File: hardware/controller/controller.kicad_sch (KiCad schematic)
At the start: 142 parts

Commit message: Update controller designs to KiCAD v7
Change-Id: I1269c7bbf32ea052580bc09d77739b31cda08142
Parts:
- C1, C10, C15, C2, C21, C22, C23, C24, C25, C3, C4, C5, C6, C7, C8: value (none) -> 0.1uF; footprint (none) -> Capacitor_SMD:C_0402_1005Metric_Pad0.74x0.62mm_HandSolder
- C11, C12, C13, C14, C16, C17, C18, C20, C9: value (none) -> 4.7uF; footprint (none) -> Capacitor_SMD:C_0603_1608Metric
- C19: value (none) -> 1pF; footprint (none) -> Capacitor_SMD:C_0402_1005Metric_Pad0.74x0.62mm_HandSolder
- D1, D2, D26, D3, D30, D31, D4, D46, D50, D51: value (none) -> D_TVS; footprint (none) -> Diode_SMD:D_SOD-323
- D10, D11, D12, D13, D14, D15, D16, D17, D18, D19, D20, D21, D22, D23, D24, D25, D27, D28, D29, D32, D33, D34, D36, D37, D38, D40, D41, D42, D43, D44, D45, D47, D48, D49, D5, D6, D7, D8, D9: value (none) -> WS2812B; footprint (none) -> LED_SMD:LED_WS2812B_PLCC4_5.0x5.0mm_P3.2mm
- D35: value (none) -> GREEN; footprint (none) -> LED_SMD:LED_0603_1608Metric
- D39: value (none) -> RED; footprint (none) -> LED_SMD:LED_0603_1608Metric
- H1, H2, H3, H4: value (none) -> MountingHole; footprint (none) -> MountingHole:MountingHole_3.2mm_M3
- J1: value (none) -> Conn_01x05; footprint (none) -> Connector_PinHeader_2.54mm:PinHeader_1x05_P2.54mm_Vertical
- J2, J5: value (none) -> Conn_01x03; footprint (none) -> Connector_PinHeader_2.54mm:PinHeader_1x03_P2.54mm_Horizontal
- J3: value (none) -> Conn_01x04; footprint (none) -> Connector_PinHeader_2.54mm:PinHeader_1x04_P2.54mm_Vertical
- J4: value (none) -> USB_B_Micro; footprint (none) -> homebrew:FRAMATOME_10118194-0001LF_fixed_bridges
- JP1, JP2: value (none) -> SolderJumper_2_Open; footprint (none) -> Jumper:SolderJumper-2_P1.3mm_Open_RoundedPad1.0x1.5mm
- L1: value (none) -> 10nH; footprint (none) -> Inductor_SMD:L_0402_1005Metric
- R1, R11, R25, R35, R7: value (none) -> 33R; footprint (none) -> Resistor_SMD:R_0603_1608Metric
- R10, R13, R6: value (none) -> 100R; footprint (none) -> Resistor_SMD:R_0603_1608Metric
- R12, R14, R15, R16, R17, R18, R22, R23, R24: value (none) -> 0R; footprint (none) -> Resistor_SMD:R_0603_1608Metric
- R19, R26, R3: value (none) -> 47k; footprint (none) -> Resistor_SMD:R_0603_1608Metric
- R2: value (none) -> 470k; footprint (none) -> Resistor_SMD:R_0603_1608Metric
- R20, R27, R34, R4: value (none) -> 24k; footprint (none) -> Resistor_SMD:R_0603_1608Metric
- R21, R28, R5: value (none) -> 68k; footprint (none) -> Resistor_SMD:R_0603_1608Metric
- R29: value (none) -> 62k; footprint (none) -> Resistor_SMD:R_0603_1608Metric
- R30: value (none) -> 180k; footprint (none) -> Resistor_SMD:R_0603_1608Metric
- R31, R32: value (none) -> 1k; footprint (none) -> Resistor_SMD:R_0603_1608Metric
- R33: value (none) -> 3k3; footprint (none) -> Resistor_SMD:R_0603_1608Metric
- R8: value (none) -> 240k; footprint (none) -> Resistor_SMD:R_0603_1608Metric
- R9: value (none) -> 680k; footprint (none) -> Resistor_SMD:R_0603_1608Metric
- S1: value (none) -> OS103011MS8QP1; footprint (none) -> snapeda:OS102011MS8QP1
- SW1, SW2, SW3, SW4, SW5, SW6, SW7, SW8, SW9: value (none) -> ILS_TA180_50; footprint (none) -> homebrew:SW_CK_TA
- SW10: value (none) -> SW_SPDT; footprint (none) -> homebrew:ANR11R11P2HQE
- TH1: value (none) -> Thermistor_PTC; footprint (none) -> Fuse:Fuse_1206_3216Metric_Pad1.42x1.75mm_HandSolder
- U1, U3, U4: value (none) -> WS2811; footprint (none) -> Package_SO:SOP-8_3.9x4.9mm_P1.27mm
- U2: value (none) -> STM32F103C8Tx; footprint (none) -> Package_QFP:LQFP-48_7x7mm_P0.5mm
- U5: value (none) -> HT75xx-1-SOT89; footprint (none) -> Package_TO_SOT_SMD:SOT-89-3
- U6: value (none) -> RFM69CW-915MHZ; footprint (none) -> homebrew:RFM69CW-minimalpads
- U7: value (none) -> TP4056; footprint (none) -> snapeda:SOP127P600X175-9N

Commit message: Schematic update for controller v1.1:
- Switch to WS2812C (low-power)
- Switch to JLC-placed TVS diodes
- Actually connect mode switch to micro
- Switch to STM32G070
- Reduce filter caps on analog buttons
- Add microphone
- Add FRAM
- Fix charge status LEDs
- Change to smaller power switch
- Add reset button
- Remove unneeded resistors on button LEDs
- Switch to smaller CH340X

Change-Id: I1a39cd43177c431c6a7b54ff1605266b9eb21616
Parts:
- removed C21, C22: 0.1uF, Capacitor_SMD:C_0402_1005Metric_Pad0.74x0.62mm_HandSolder, symbol Device:C
- removed D46, D50, D51: D_TVS, Diode_SMD:D_SOD-323, symbol Device:D_TVS
- removed JP1, JP2: SolderJumper_2_Open, Jumper:SolderJumper-2_P1.3mm_Open_RoundedPad1.0x1.5mm, symbol Jumper:SolderJumper_2_Open
- removed R16, R17, R18, R22, R23, R24: 0R, Resistor_SMD:R_0603_1608Metric, symbol Device:R
- removed R34: 24k, Resistor_SMD:R_0603_1608Metric, symbol Device:R
- removed SW10: SW_SPDT, homebrew:ANR11R11P2HQE, symbol Switch:SW_SPDT
- removed U2: STM32F103C8Tx, Package_QFP:LQFP-48_7x7mm_P0.5mm, symbol MCU_ST_STM32F1:STM32F103C8Tx
- added C21, C22, C28: 100uF, Capacitor_SMD:CP_Elec_6.3x5.4, symbol Device:C_Polarized
- added C26, C27, C29, C30, C31, C32, C33, C34, C35, C36, C37, C38, C39, C40, C41, C42, C43, C44, C45, C46, C47, C48, C49, C50, C51, C52, C53, C54, C55, C56, C57, C58, C59, C60, C61, C62, C63, C64, C65, C66, C67: 100nF, Capacitor_SMD:C_0402_1005Metric_Pad0.74x0.62mm_HandSolder, symbol Device:C
- added D46: SRV05-4-P-T7, Package_TO_SOT_SMD:SOT-23-6, symbol Homebrew:SRV05-4-P-T7
- added D52: D, Diode_SMD:D_SMA, symbol Device:D
- added J6: Conn_01x02, Homebrew:JST_Micro_1x02_P1.25mm_Horizontal, symbol Connector_Generic:Conn_01x02
- added MK1: Microphone, Homebrew:MIC_CMA-4544PF-W, symbol Device:Microphone
- added Q1: MMBT2222A 1P, Package_TO_SOT_SMD:SOT-23, symbol Transistor_BJT:MMBT3904
- added Q2: AO3400A, Package_TO_SOT_SMD:SOT-23, symbol Transistor_FET:AO3400A
- added R36: 1k, Resistor_SMD:R_0603_1608Metric, symbol Device:R
- added R38, R39: 220, Resistor_SMD:R_0402_1005Metric, symbol Device:R
- added R40, R41: 3k3, Resistor_SMD:R_0603_1608Metric, symbol Device:R
- added R42, R44: 2k2, Resistor_SMD:R_0603_1608Metric_Pad0.98x0.95mm_HandSolder, symbol Device:R
- added R43: 6k8, Resistor_SMD:R_0603_1608Metric_Pad0.98x0.95mm_HandSolder, symbol Device:R
- added R45: 220, Resistor_SMD:R_0603_1608Metric_Pad0.98x0.95mm_HandSolder, symbol Device:R
- added R46: 1k, Resistor_SMD:R_0603_1608Metric_Pad0.98x0.95mm_HandSolder, symbol Device:R
- added SW10: SW_Push, Homebrew:SW_TACTILE_5.1MM_TS-1187A-C-D-B, symbol Switch:SW_Push
- added SW11: SW_DPDT_x2, Homebrew:SK22D15L5_SP, symbol Switch:SW_DPDT_x2
- added U10: CH340X, Package_SO:MSOP-10_3x3mm_P0.5mm, symbol Interface_USB:CH340E
- added U2: FM24CL16B, Package_SO:SOIC-8_3.9x4.9mm_P1.27mm, symbol Memory_NVRAM:FM24CL16B
- added U8: STM32G070CBTx, Package_QFP:LQFP-48_7x7mm_P0.5mm, symbol MCU_ST_STM32G0:STM32G070CBTx
- C1, C10, C15, C23, C25, C3, C5, C6, C7: value 0.1uF -> 100nF
- C11, C12, C13, C14, C16, C17, C18, C9: value 4.7uF -> 10uF; LCSC C19666 -> C96446
- C2, C4, C8: value 0.1uF -> 22nF; LCSC C307331 -> C1532
- C20: value 4.7uF -> 100nF; footprint Capacitor_SMD:C_0603_1608Metric -> Capacitor_SMD:C_0402_1005Metric_Pad0.74x0.62mm_HandSolder; LCSC C19666 -> C307331
- C24: value 0.1uF -> 10nF; footprint Capacitor_SMD:C_0402_1005Metric_Pad0.74x0.62mm_HandSolder -> Capacitor_SMD:C_0603_1608Metric_Pad1.08x0.95mm_HandSolder; LCSC C307331 -> C85973
- D1, D2, D26, D3, D30, D31, D4: LCSC (none) -> C127522; MPN DESD5V0U1BA-7 -> (none)
- D10, D11, D12, D13, D14, D15, D16, D17, D18, D19, D20, D21, D22, D23, D24, D25, D27, D28, D29, D32, D33, D34, D36, D37, D38, D40, D41, D42, D43, D44, D45, D47, D48, D49, D5, D6, D7, D8, D9: value WS2812B -> WS2812C/W; LCSC C2761795 -> C2761796
- D35: value GREEN -> WHITE; LCSC (none) -> C2290; MPN LTST-C190KGKT -> (none)
- R1, R11, R25, R35, R7: value 33R -> 33
- R10, R13, R6: value 100R -> 100
- R12: value 0R -> 220; footprint Resistor_SMD:R_0603_1608Metric -> Resistor_SMD:R_0402_1005Metric; LCSC C21189 -> C25091
- R14: value 0R -> 10k; footprint Resistor_SMD:R_0603_1608Metric -> Resistor_SMD:R_0402_1005Metric; LCSC C21189 -> C25744
- R15: value 0R -> 4k7; footprint Resistor_SMD:R_0603_1608Metric -> Resistor_SMD:R_0402_1005Metric; LCSC C21189 -> C25900
- S1: footprint snapeda:OS102011MS8QP1 -> OS102011MS8QP1
- TH1: footprint Fuse:Fuse_1206_3216Metric_Pad1.42x1.75mm_HandSolder -> Fuse:Fuse_0805_2012Metric; LCSC (none) -> C269105; MPN PTS12066V100 -> (none)
- U6: footprint homebrew:RFM69CW-minimalpads -> RFM69CW-XXXS2
- U7: footprint snapeda:SOP127P600X175-9N -> SOP127P600X175-9N
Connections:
- net SWCLK is gone; now on net BOOT0: J3.4 (Pin_4)
- net +BATT: now also J5.3 (Pin_3), C29.1, C30.1, C31.1, C32.1, C33.1, C34.1, C35.1, C36.1, C37.1, C38.1, C39.1, C40.1, C41.1, C42.1, C43.1, C44.1, C45.1, C46.1, C47.1, C48.1, C49.1, C50.1, C51.1, C52.1, C53.1, C54.1, C55.1, C56.1, C57.1, C58.1, C59.1, C60.1, C61.1, C62.1, C63.1, C64.1, C65.1, C66.1, C67.1, D52.1 (K), SW11.1 (A), SW11.4 (A); no longer J5.1 (Pin_1)
- net AUX0: now also J1.4 (Pin_4), U8.22 (PB10); no longer J1.2 (Pin_2)
- net AUX1: now also J1.5 (Pin_5), U8.23 (PB11); no longer J1.1 (Pin_1)
- net BATT_DIRECT: now also SW11.2 (B), SW11.5 (B)
- net BLED_0: now also U1.1 (OUTR); no longer R12.1
- net BLED_1: now also U1.2 (OUTG); no longer R14.1
- net BLED_2: now also U1.3 (OUTB)
- net BLED_3: now also U3.3 (OUTB)
- net BLED_4: now also U3.2 (OUTG)
- net BLED_5: now also U3.1 (OUTR); no longer R15.1
- net BLED_6: now also U4.2 (OUTG)
- net BLED_7: now also U4.1 (OUTR)
- net BLED_8: now also U4.3 (OUTB)
- net BOOT0: now also U10.4 (~{RTS}), U8.36 (PA14); no longer C24.2
- net DIO0: now also U8.20 (PB1)
- net GND: now also C1.2, C20.2, J1.1 (Pin_1), J5.1 (Pin_1), R14.1, C27.2, C29.2, C30.2, C31.2, C32.2, C33.2, C34.2, C35.2, C36.2, C37.2, C38.2, C39.2, C40.2, C41.2, C42.2, C43.2, C44.2, C45.2, C46.2, C47.2, C48.2, C49.2, C50.2, C51.2, C52.2, C53.2, C54.2, C55.2, C56.2, C57.2, C58.2, C59.2, C60.2, C61.2, C62.2, C63.2, C64.2, C65.2, C66.2, C67.2, D46.2 (GND), D52.2 (A), J6.1 (Pin_1), Q2.2 (S), SW10.1, U10.3 (GND), U2.4 (VSS), U8.7 (VSS); no longer C1.1, C20.1, C24.1, J1.5 (Pin_5), J5.3 (Pin_3)
- net LED_OUT: now also U8.15 (PA4)
- net MISO: now also U8.43 (PB4)
- net MOSI: now also U8.44 (PB5)
- net NSS: now also U8.19 (PB0)
- net SCK: now also U8.42 (PB3)
- net SWDIO: now also U8.35 (PA13)
- net SW_ACTION: now also U8.16 (PA5)
- net SW_LEFT: now also U8.11 (PA0)
- net SW_MODE: now also U8.17 (PA6)
- net SW_RIGHT: now also U8.12 (PA1)
- net USB+: now also D46.1 (IO1), U10.1 (UD+)
- net USB-: now also D46.3 (IO2), U10.2 (UD-)
- net VBATT_DIV: now also U8.18 (PA7)
- net VBUS: now also D39.2 (A), D46.5 (REF), R36.1
- net VCC: now also C1.1, C20.1, J1.2 (Pin_2), C27.1, C28.1, R40.1, R41.1, R42.1, R43.1, R46.1, U10.10 (V3), U10.7 (VCC), U2.8 (VDD), U8.5 (VREF+), U8.6 (VDD); no longer C20.2, J1.4 (Pin_4)
- net at R12.2: now also R14.2, Q2.1 (G); no longer U1.1 (OUTR)
- net at J2.3 (Pin_3), TH1.2: now also J6.2 (Pin_2)
- net at R15.2: now also U10.5 (~{CTS}); no longer U3.1 (OUTR)
- net at U7.8 (CE): now also R36.2; no longer D39.2 (A)
- new net: C26.1, SW10.2, U8.10 (NRST)
- new net: R39.1, U10.9 (RXD)
- new net: R38.1, U10.8 (TXD)
- new net: C21.2, C24.1, Q1.1 (B), R43.2, R44.1
- new net: C22.1, Q1.2 (E), R45.1
- new net: C22.2, C28.2, MK1.1 (-), Q2.3 (D), R44.2, R45.2
- new net: SW11.3 (C), SW11.6 (C)
- new net: C21.1, MK1.2 (+), R42.2
- new net MIC_ENABLE: R12.1, U8.25 (PB13)
- new net MIC_OUT: C24.2, Q1.3 (C), R46.2, U8.24 (PB12)
- new net SCL: R41.2, U2.6 (SCL), U8.29 (PA9/NC)
- new net SDA: R40.2, U2.5 (SDA), U8.32 (PA10/NC)
- new net USART_RX: R38.2, U8.14 (PA3)
- new net USART_TX: R39.2, U8.13 (PA2)
- new net ~{DTR}: C26.2, R15.1, U10.6 (TNOW)
- no-connect marks 53 -> 56
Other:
- note added: "750mA"
- note added: "FRAM"
- note added: "MIC"
- note added: "SPI1"
- note added: "SPI2"
- moved on the sheet: C12, C15, C16, C19, C23, C9, D26, J2, J4, L1, TH1, U6

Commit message: Controller PCB version 1.1
Change-Id: I1cbaa3f158fa0af12788e3f52120070e6be7d808
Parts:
- removed C2, C4, C8: 22nF, Capacitor_SMD:C_0402_1005Metric_Pad0.74x0.62mm_HandSolder, symbol Device:C
- removed D3: D_TVS, Diode_SMD:D_SOD-323, symbol Device:D_TVS
- removed R21, R28: 68k, Resistor_SMD:R_0603_1608Metric, symbol Device:R
- removed R26: 47k, Resistor_SMD:R_0603_1608Metric, symbol Device:R
- removed R27: 24k, Resistor_SMD:R_0603_1608Metric, symbol Device:R
- removed SW11: SW_DPDT_x2, Homebrew:SK22D15L5_SP, symbol Switch:SW_DPDT_x2
- added D50, D51, D53, D54, D55, D56, D57: D_TVS, Diode_SMD:D_SOD-323, symbol Device:D_TVS
- added R16, R17, R18: 1k, Resistor_SMD:R_0402_1005Metric, symbol Device:R
- added SW11: SW_SPDT, Homebrew:SW_SPDT_SK-12D02-G060, symbol Switch:SW_SPDT
- added U9: ISL29125, Sparkfun_Silicon_Standard:ODFN-6, symbol SparkFun_Sensors:ISL29125
- J5: footprint Connector_PinHeader_2.54mm:PinHeader_1x03_P2.54mm_Horizontal -> Connector_PinHeader_2.54mm:PinHeader_1x03_P2.54mm_Vertical
- R11: value 33 -> 1k; footprint Resistor_SMD:R_0603_1608Metric -> Resistor_SMD:R_0402_1005Metric; LCSC C23140 -> C11702
- R19, R3: value 47k -> 1k; footprint Resistor_SMD:R_0603_1608Metric -> Resistor_SMD:R_0402_1005Metric; LCSC C25819 -> C11702
- R20, R4: value 24k -> 1k; footprint Resistor_SMD:R_0603_1608Metric -> Resistor_SMD:R_0402_1005Metric; LCSC C23352 -> C11702
- R31, R32, R36: footprint Resistor_SMD:R_0603_1608Metric -> Resistor_SMD:R_0402_1005Metric; LCSC C21190 -> C11702
- R5: value 68k -> 1k; footprint Resistor_SMD:R_0603_1608Metric -> Resistor_SMD:R_0402_1005Metric; LCSC C23231 -> C11702
- SW1, SW2, SW3, SW4, SW5, SW6, SW7, SW8, SW9: footprint homebrew:SW_CK_TA -> Homebrew:SW_CK_TA
- U7: footprint SOP127P600X175-9N -> Homebrew:SOP127P600X175-9N
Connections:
- net +BATT: now also SW11.3 (C)
- net BATT_DIRECT: now also SW11.2 (B)
- net GND: now also C20.1, D50.1 (A1), D51.1 (A1), D53.1 (A1), D54.1 (A1), D55.1 (A1), D56.1 (A1), D57.1 (A1), U9.3 (GND); no longer C20.2
- net SCL: now also U9.6 (SCL)
- net SDA: now also U9.4 (SDA)
- net VCC: now also C20.2, U9.1 (VDD); no longer C20.1, R19.2, R3.2
- net at D23.2 (DOUT): now also D49.4 (DIN); no longer D27.4 (DIN)
- net at U4.6 (DIN): now also R25.1; no longer R11.1
- net at D49.2 (DOUT): now also D48.4 (DIN); no longer R11.2
- net at D47.4 (DIN): now also D48.2 (DOUT); no longer R25.1
- net at SW4.2: now also R11.1
- net at SW5.1: now also R17.2; no longer R20.1
- net at SW6.1: now also R18.2
- net at SW8.1: now also R19.2
- net at SW9.1: now also R20.2
- net at D47.2 (DOUT): now also D27.4 (DIN); no longer D48.4 (DIN)
- net SW_LEFT1: now reaches U8.21 (PB2)
- net SW_LEFT1: now also D1.2 (A2), R3.1
- net SW_LEFT2: now reaches U8.26 (PB14)
- net SW_LEFT2: now also R4.1, D50.2 (A2)
- net SW_LEFT3: now reaches U8.27 (PB15)
- net SW_LEFT3: now also R5.1, D51.2 (A2)
- net SW_RIGHT1: now reaches U8.28 (PA8)
- net SW_RIGHT1: now also D4.2 (A2), R11.2
- net SW_RIGHT2: now reaches U8.30 (PC6)
- net SW_RIGHT2: now also D54.2 (A2), R17.1
- net SW_RIGHT3: now reaches U8.31 (PC7)
- net SW_RIGHT3: now also D55.2 (A2), R18.1
- net SW_ACTION1: now reaches U8.33 (PA11/PA9)
- net SW_ACTION1: now also D53.2 (A2), R16.1
- net SW_ACTION2: now reaches U8.34 (PA12/PA10)
- net SW_ACTION2: now also R19.1, D56.2 (A2)
- net SW_ACTION3: now reaches U8.37 (PA15)
- net SW_ACTION3: now also R20.1, D57.2 (A2)
- removed net SW_ACTION: D4.2 (A2), SW7.1, U8.16 (PA5)
- removed net SW_LEFT: D1.2 (A2), R3.1, R4.2, SW1.1, U8.11 (PA0)
- removed net SW_RIGHT: R19.1, R20.2, SW4.1, U8.12 (PA1)
- new net: R3.2, SW1.1
- new net: R4.2, SW2.1
- new net: R16.2, SW7.1
- no-connect marks 56 -> 52
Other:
- note added: "LIGHT SENSOR"
- moved on the sheet: C3, C5, C6, D1, D10, D11, D12, D13, D14, D15, D16, D17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

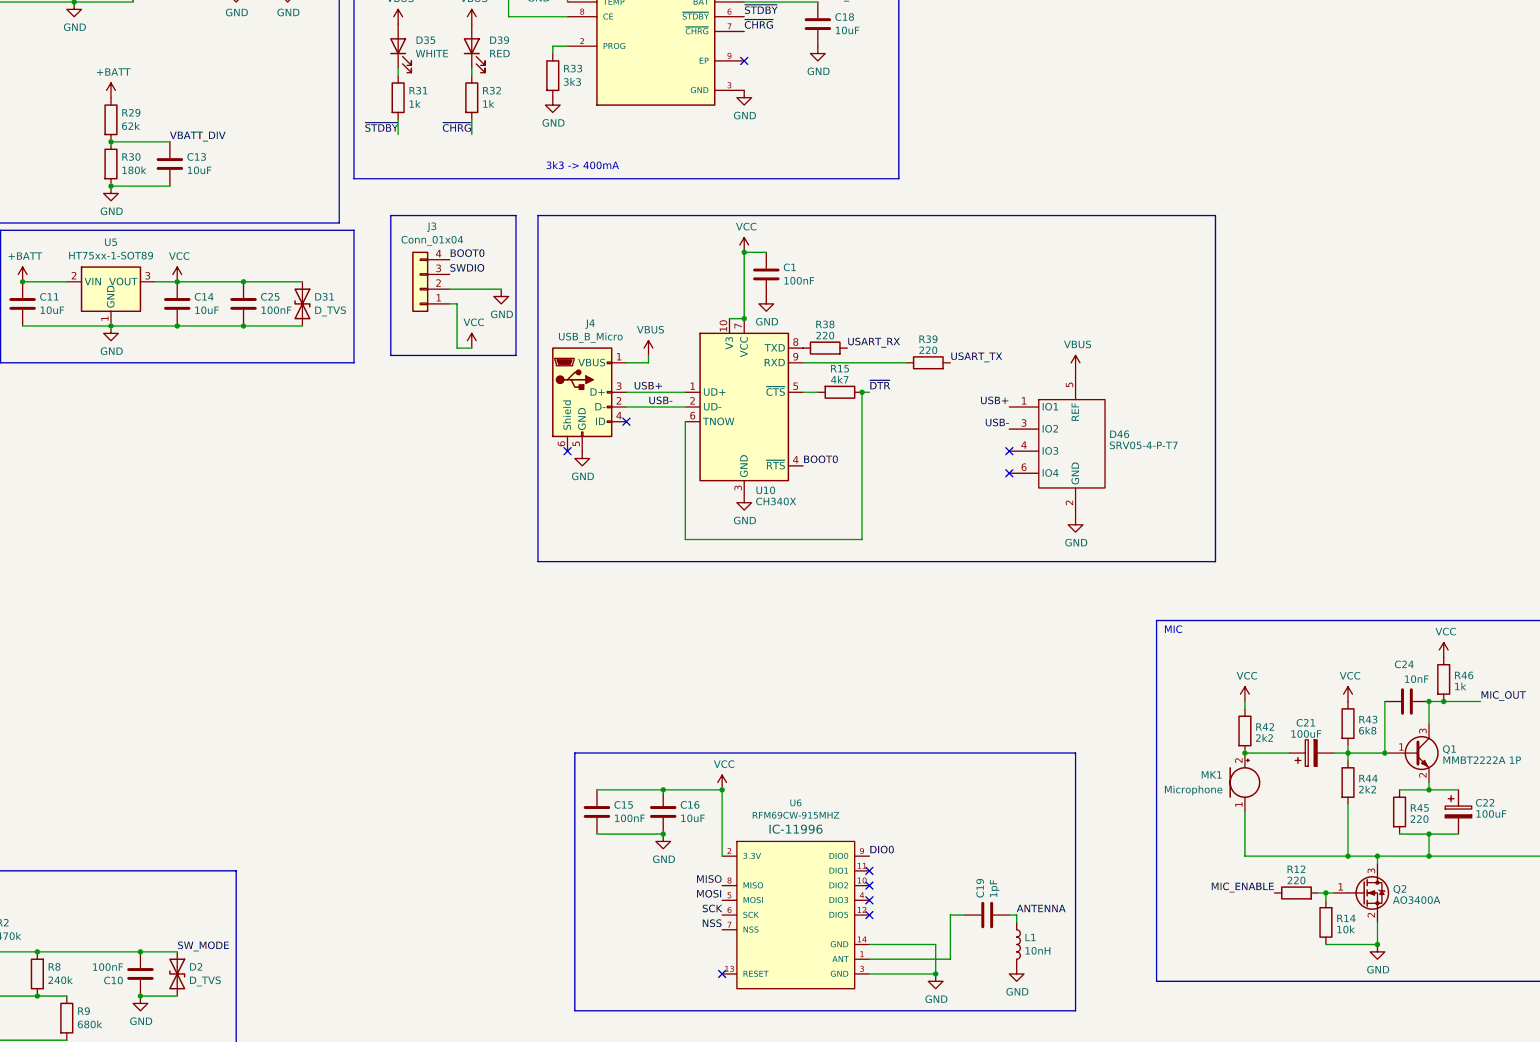
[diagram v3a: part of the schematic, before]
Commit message: Cost optimizations for controller v1.1
This consolidates some of the resistors values to reduce the number of
BOM line items.

Change-Id: Ia3d1077ce7e82b015c1ec4700b90b76e07124758
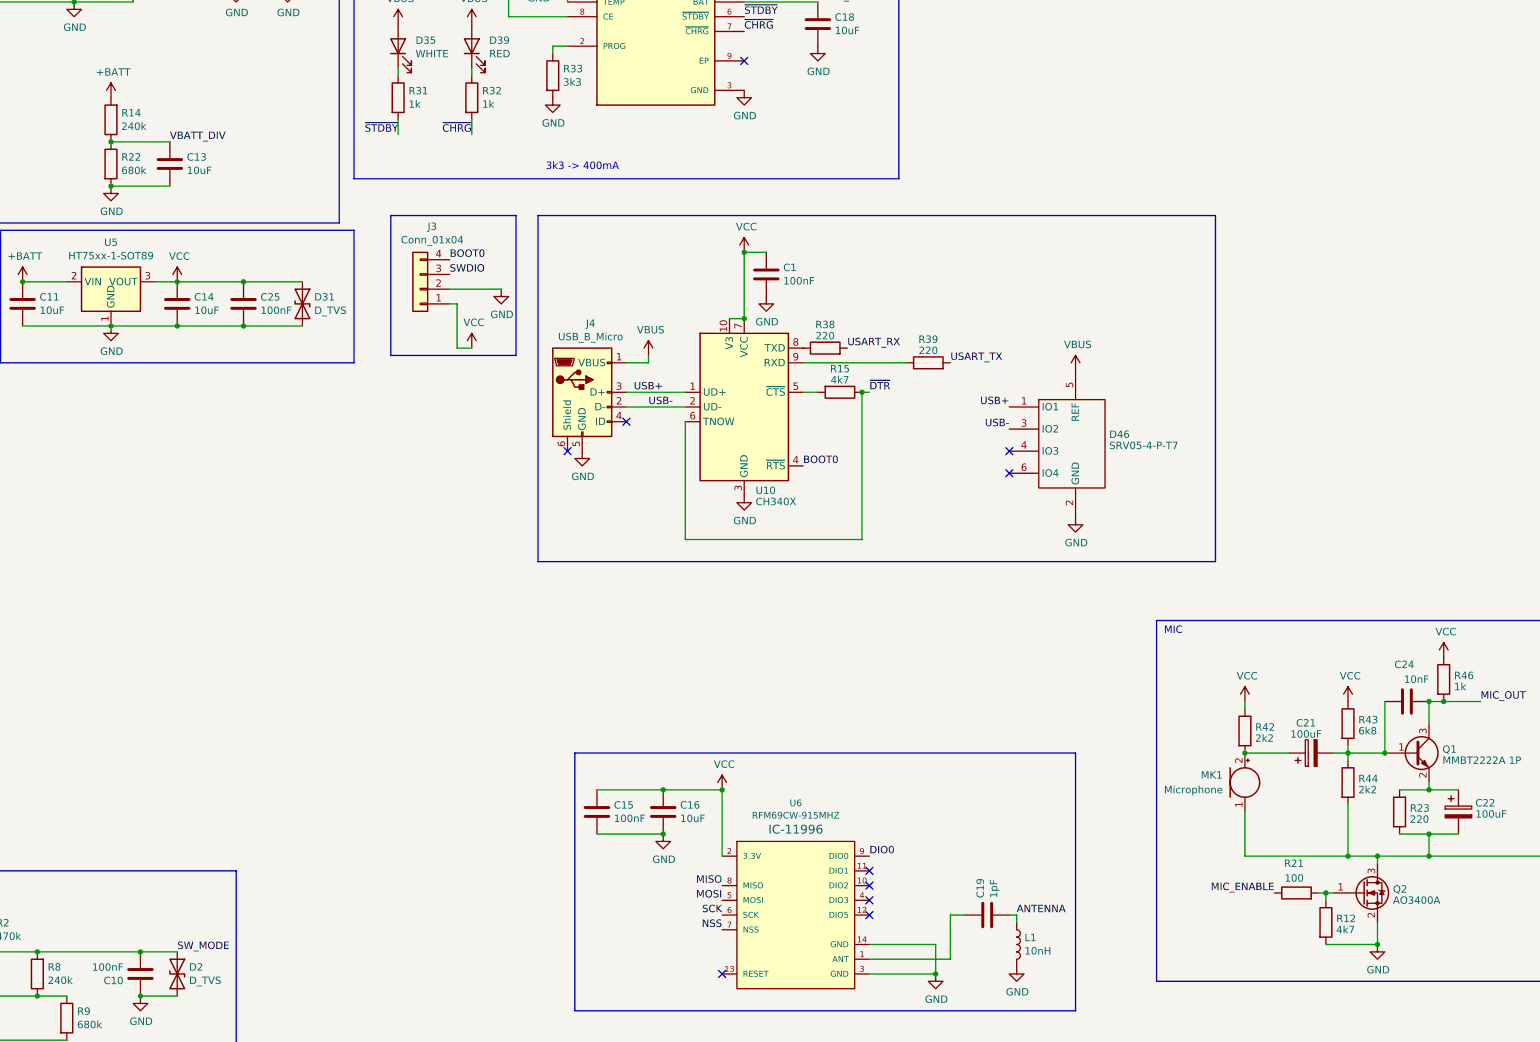
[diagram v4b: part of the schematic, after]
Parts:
- removed R29: 62k, Resistor_SMD:R_0603_1608Metric, symbol Device:R
- removed R30: 180k, Resistor_SMD:R_0603_1608Metric, symbol Device:R
- removed R45: 220, Resistor_SMD:R_0603_1608Metric_Pad0.98x0.95mm_HandSolder, symbol Device:R
- added R21: 100, Resistor_SMD:R_0402_1005Metric, symbol Device:R
- added R22: 680k, Resistor_SMD:R_0603_1608Metric, symbol Device:R
- added R23: 220, Resistor_SMD:R_0402_1005Metric, symbol Device:R
- R10, R13, R6: footprint Resistor_SMD:R_0603_1608Metric -> Resistor_SMD:R_0402_1005Metric; LCSC C22775 -> C25076
- R12: value 220 -> 4k7; LCSC C25091 -> C25900
- R14: value 10k -> 240k; footprint Resistor_SMD:R_0402_1005Metric -> Resistor_SMD:R_0603_1608Metric; LCSC C25744 -> C4197
- R46: footprint Resistor_SMD:R_0603_1608Metric_Pad0.98x0.95mm_HandSolder -> Resistor_SMD:R_0402_1005Metric; LCSC C21190 -> C11702
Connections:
- net +BATT: now also R14.2
- net GND: now also R12.2, R22.2; no longer R14.1
- net MIC_ENABLE: now also R21.1; no longer R12.1
- net VBATT_DIV: now also R14.1, R22.1
- net at C22.1, Q1.2 (E): now also R23.2
- net at C22.2, C28.2, MK1.1 (-)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: now also R23.1
- new net: Q2.1 (G), R12.1, R21.2
